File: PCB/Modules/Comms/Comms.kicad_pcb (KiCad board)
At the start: 4 copper layers, 50 x 50 mm, 26 parts, among them J1 In, J2 ESP32, J3 Bus, J4 Bus, SW1 RUN/~{PROG}, U1 DS1390U, U2 THVD1420D, U3 WiFi / BLE, Y1 32.767kHz

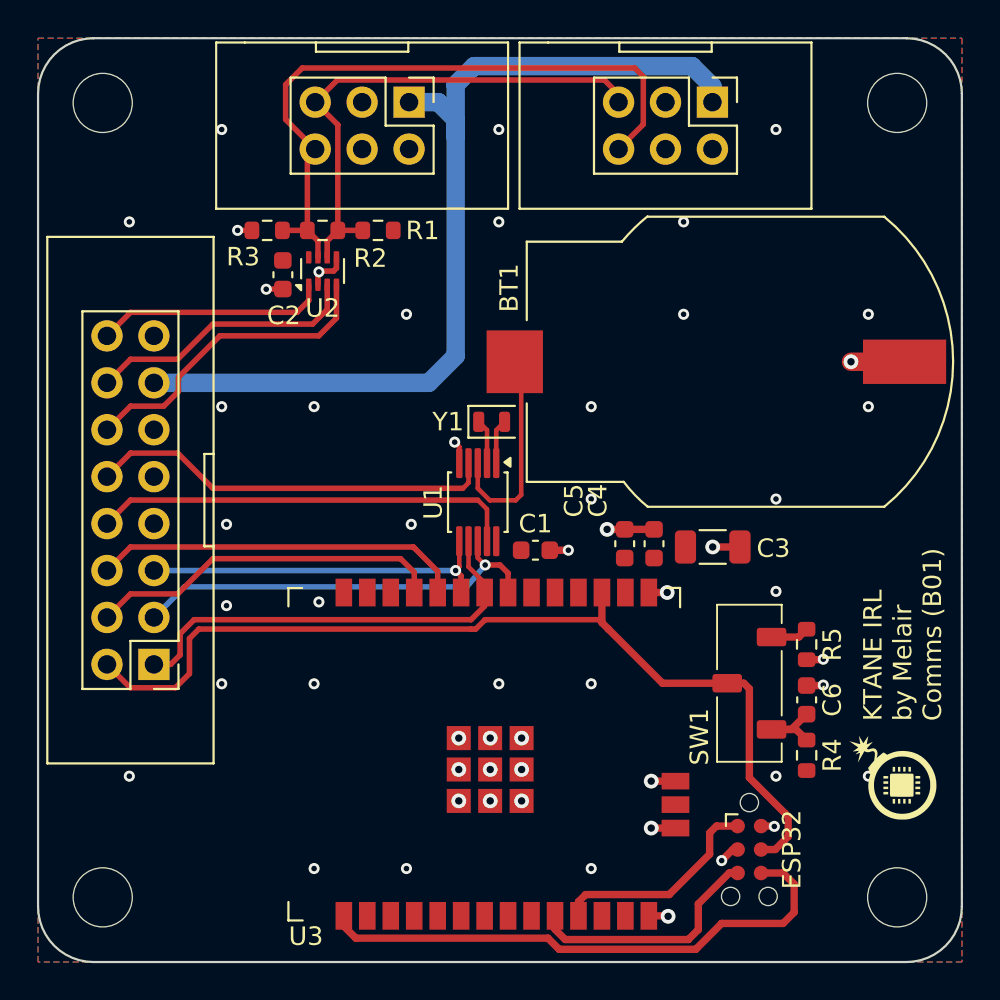
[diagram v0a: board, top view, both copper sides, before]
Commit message: Add ESD protection to the RS485 networks.
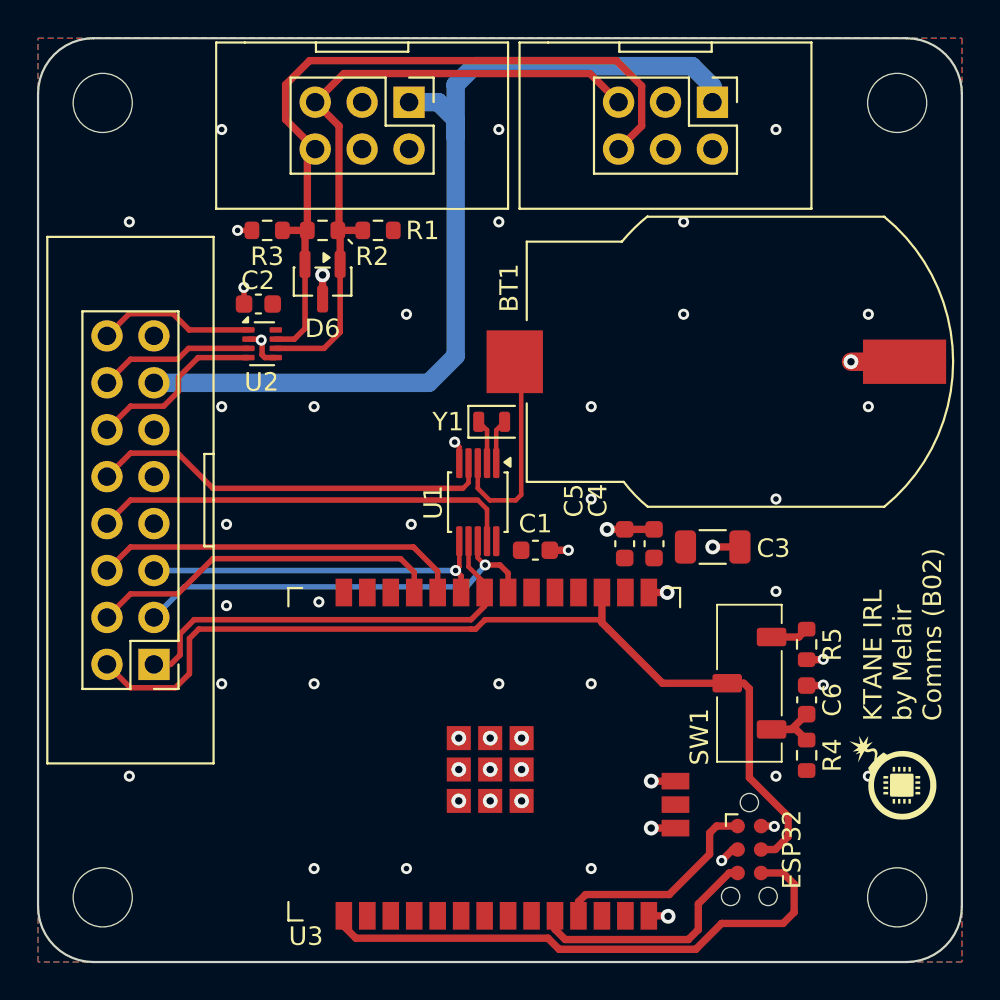
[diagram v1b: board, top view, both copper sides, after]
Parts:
- added D6: T24CAN, Package_TO_SOT_SMD:SOT-23, F.Cu at (35.4, 33.2)
- R1, R3: value 470 -> 430
- moved U2 5.12 mm to (32.1, 36.5), turned to 0 degrees
- moved C2 2.07 mm to (31.9, 34.4), turned to 180 degrees
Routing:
- net A: track 28.2 -> 36.0 mm
- net BUS-TX: track 17.2 -> 9.72 mm
- net BUS-DE: track 14.9 -> 8.43 mm
- net B: track 36.2 -> 41.6 mm
- net BUS-RX: track 12.6 -> 8.52 mm
- net GND: track 20.8 -> 22.1 mm, vias 37 -> 38
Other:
- board text added: "KTANE IRL by Melair Comms (B02)"
- board text removed: "KTANE IRL by Melair Comms (B01)"

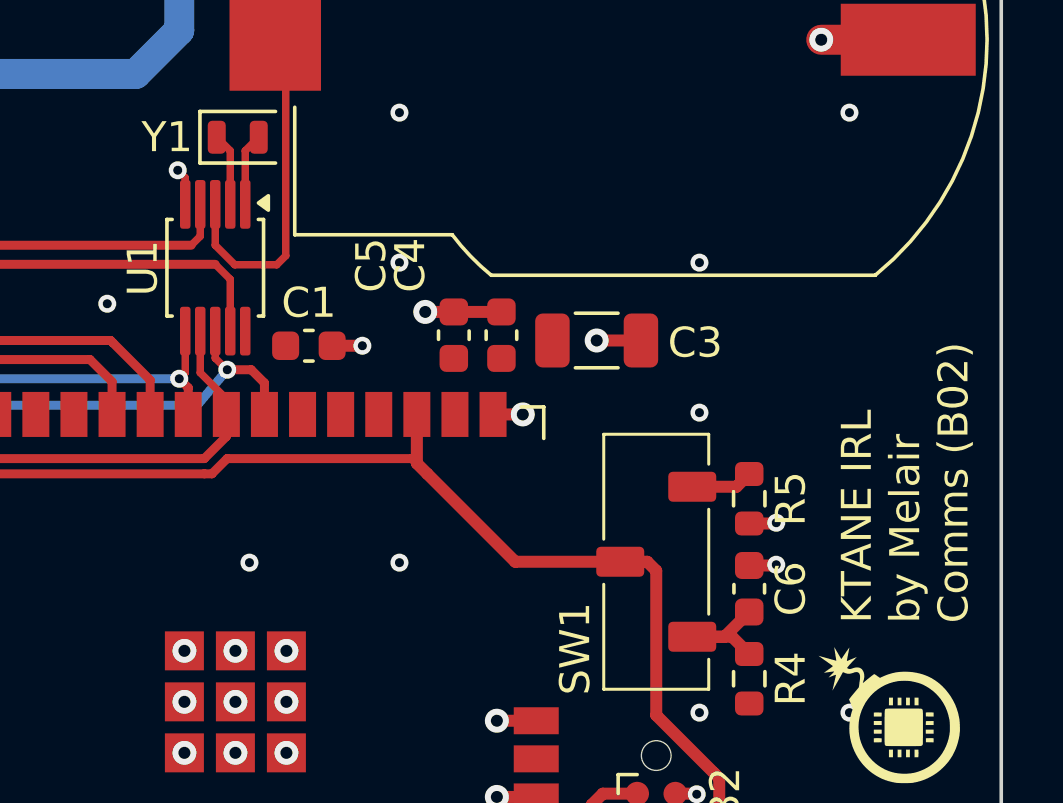
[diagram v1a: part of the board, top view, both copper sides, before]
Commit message: Include all corrections, mint new gerbers. Update some to KiCad 10.
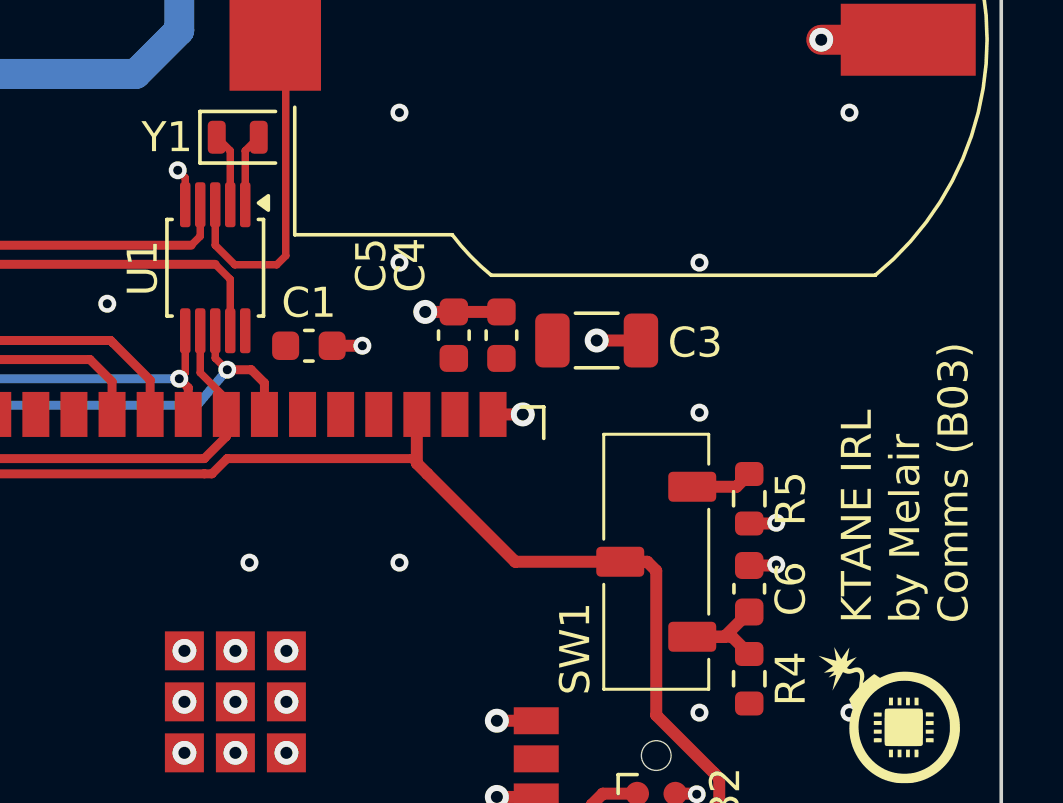
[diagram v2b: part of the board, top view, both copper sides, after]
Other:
- board text added: "KTANE IRL by Melair Comms (B03)"
- board text removed: "KTANE IRL by Melair Comms (B02)"

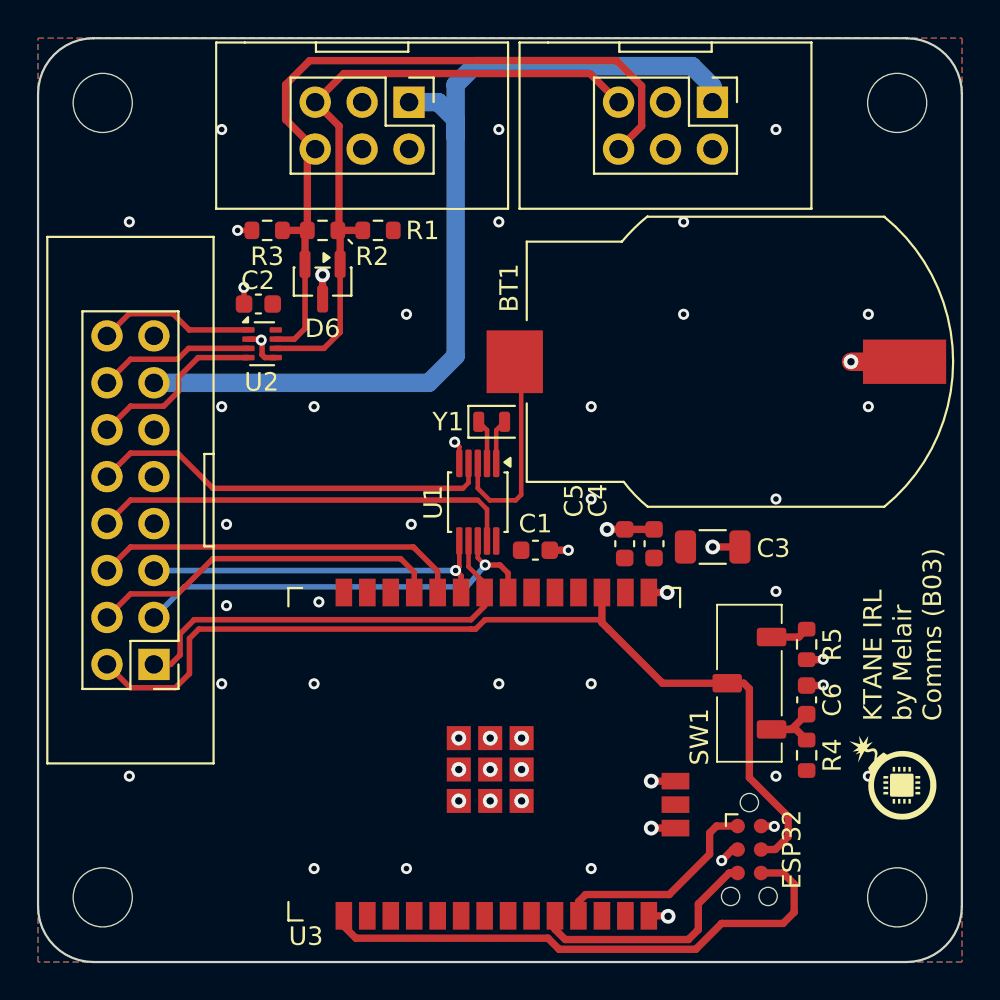
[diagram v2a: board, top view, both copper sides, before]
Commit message: feat: Rework comms board to have an STM32 for communications.
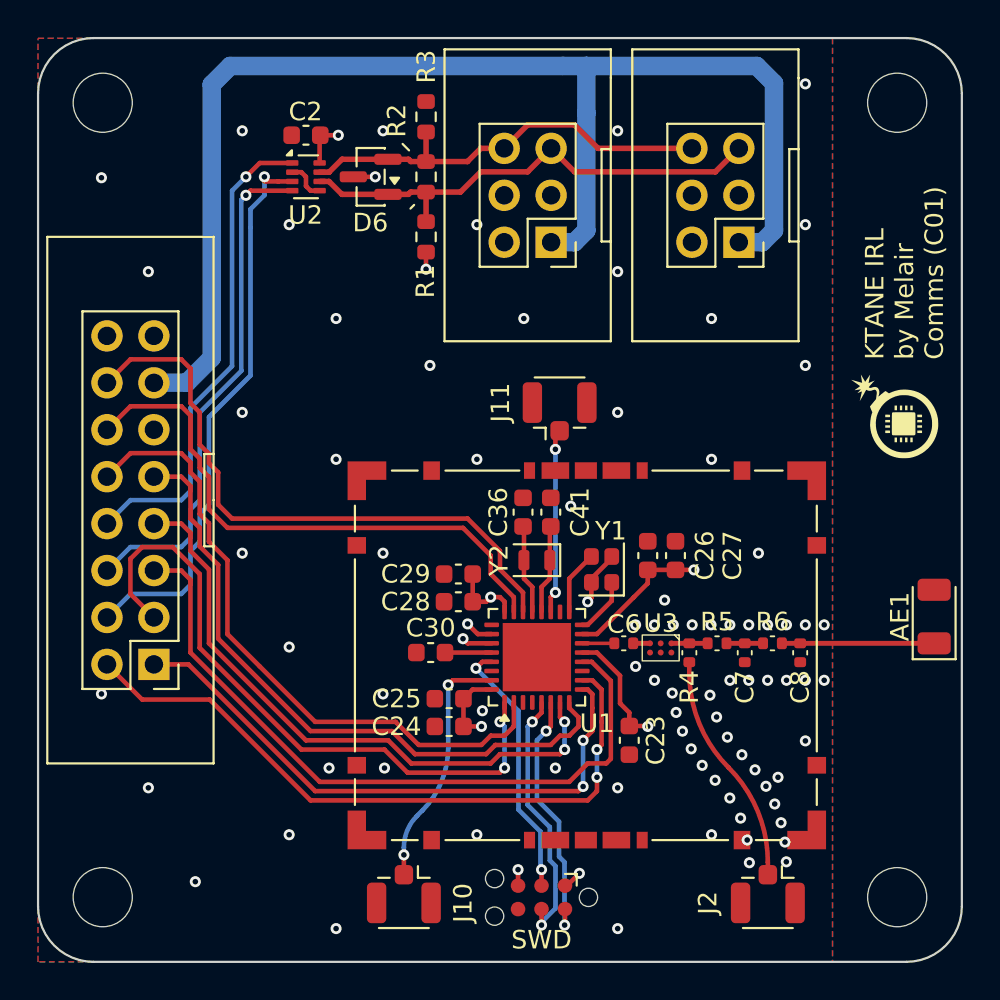
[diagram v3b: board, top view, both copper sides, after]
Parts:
- removed BT1: CR2032, KTANE:CellHolder
- removed C1: 0.1μF, Capacitor_SMD:C_0603_1608Metric
- removed C3: 22uF, Capacitor_SMD:C_1206_3216Metric
- removed C4: 47uF, Capacitor_SMD:C_0603_1608Metric
- removed C5: 0.1uF, Capacitor_SMD:C_0603_1608Metric
- removed SW1: RUN/~{PROG}, KTANE:JS102011JCQN
- added AE1: 2450AT18A0100001E, RF_Antenna:Johanson_2450AT18x100_2400-2500Mhz, F.Cu at (68.5, 51.3)
- added C23: 0.1μF, Capacitor_SMD:C_0603_1608Metric, F.Cu at (52.0, 58.0)
- added C24: 0.1μF, Capacitor_SMD:C_0603_1608Metric, F.Cu at (42.2, 57.2)
- added C25: 4.7uF, Capacitor_SMD:C_0603_1608Metric, F.Cu at (42.2, 55.8)
- added C26: 0.1μF, Capacitor_SMD:C_0603_1608Metric, F.Cu at (53.0, 48.0)
- added C27: 100pF, Capacitor_SMD:C_0603_1608Metric, F.Cu at (54.5, 48.0)
- added C28: 0.1μF, Capacitor_SMD:C_0603_1608Metric, F.Cu at (42.8, 50.5)
- added C29: 4.7uF, Capacitor_SMD:C_0603_1608Metric, F.Cu at (42.8, 49.0)
- added C30: 0.1μF, Capacitor_SMD:C_0603_1608Metric, F.Cu at (41.2, 53.2)
- added C36: 8pF, Capacitor_SMD:C_0603_1608Metric, F.Cu at (46.2, 45.6)
- added C41: 8pF, Capacitor_SMD:C_0603_1608Metric, F.Cu at (47.8, 45.6)
- added C7: ~, KTANE:R_0402_1005Metric_Tweaked, F.Cu at (58.2, 53.3)
- added C8: ~, KTANE:R_0402_1005Metric_Tweaked, F.Cu at (61.2, 53.3)
- added J10: 1PPS In, Connector_Coaxial:U.FL_Hirose_U.FL-R-SMT-1_Vertical, F.Cu at (39.8, 66.8)
- added J11: 32MHz Out, Connector_Coaxial:U.FL_Hirose_U.FL-R-SMT-1_Vertical, F.Cu at (48.2, 39.7)
- added J12: Shield, KTANE:EMI_Shield_Straight, F.Cu at (49.6, 63.4)
- added J13: Shield, KTANE:EMI_Shield_Straight, F.Cu at (49.6, 43.4)
- added J5: SWD, Connector:Tag-Connect_TC2030-IDC-NL_2x03_P1.27mm_Vertical, F.Cu at (47.2, 66.5)
- added J6: Shield, KTANE:EMI_Shield_Corner, F.Cu at (62.1, 43.4)
- added J7: Shield, KTANE:EMI_Shield_Corner, F.Cu at (37.2, 43.4)
- added J8: Shield, KTANE:EMI_Shield_Corner, F.Cu at (37.2, 63.4)
- added J9: Shield, KTANE:EMI_Shield_Corner, F.Cu at (62.1, 63.4)
- added R6: 0, KTANE:R_0402_1005Metric_Tweaked, F.Cu at (59.8, 52.8)
- added Y2: 32.768k, Crystal:Crystal_SMD_2012-2Pin_2.0x1.2mm, F.Cu at (47.0, 48.2)
- C6: value 0.1μF -> 20pF; footprint Capacitor_SMD:C_0603_1608Metric -> KTANE:R_0402_1005Metric_Tweaked
- H1, H2, H3, H4: footprint MountingHole:MountingHole_3.2mm_M3 -> KTANE:MountingHole_3.2mm_M3_NoCopper
- J2: value ESP32 -> Test; footprint Connector:Tag-Connect_TC2030-IDC-NL_2x03_P1.27mm_Vertical -> Connector_Coaxial:U.FL_Hirose_U.FL-R-SMT-1_Vertical
- R4, R5: value 10k -> 0; footprint Resistor_SMD:R_0603_1608Metric -> KTANE:R_0402_1005Metric_Tweaked
- U1: value DS1390U -> STM32WB09KEVx; footprint Package_SO:MSOP-10_3x3mm_P0.5mm -> Package_DFN_QFN:QFN-32-1EP_5x5mm_P0.5mm_EP3.7x3.7mm
- U3: value WiFi / BLE -> MLPF-NRG-01D3; footprint KTANE:ESP32-C5-WROOM-1U -> KTANE:MLPF-NRG-01D3
- Y1: value 32.767kHz -> 32MHz; footprint Crystal:Crystal_SMD_2012-2Pin_2.0x1.2mm -> Crystal:Crystal_SMD_2016-4Pin_2.0x1.6mm
- moved G*** 19.6 mm to (66.4, 40.4)
- moved U3 11.0 mm to (53.7, 53.0)
- moved R3 10.6 mm to (41.0, 24.2), turned to 90 degrees
- moved C6 10.4 mm to (51.7, 52.8), turned to 180 degrees
- moved Y1 9.96 mm to (50.5, 48.8), turned to 90 degrees
- moved J3 9.72 mm to (46.5, 28.5), turned to 180 degrees
- moved C2 9.49 mm to (34.5, 25.2)
- moved U2 9.34 mm to (34.5, 27.5)
- moved U1 8.98 mm to (47.0, 53.5), turned to 90 degrees
- moved R4 8.43 mm to (55.2, 53.3)
- moved R2 6.31 mm to (41.0, 27.5), turned to 90 degrees
- moved D6 6.24 mm to (38.0, 27.5), turned to 180 degrees
- moved R5 4.85 mm to (56.8, 52.8), turned to 0 degrees
- moved J4 4.64 mm to (56.7, 28.5), turned to 180 degrees
- moved J2 3.06 mm to (59.5, 66.8)
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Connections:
- C6 pad 1: Net-(SW1-A) -> Net-(U3-IN)
- C6 pad 2: GND -> Net-(U1-RF1)
- J1 pad 10: ~{RTC-CS} -> ~{BLE_INT}
- J1 pad 12: BUS-TX -> BLE-UART-TX
- J1 pad 14: BUS-DE -> BLE-UART-RX
- J1 pad 16: BUS-RX -> unconnected-(J1-I7-Pad16)
- J1 pad 2: ESP32-EN -> ~{SPI-CS}
- J1 pad 4: ~{ESP32-INT} -> BUS-DE
- J1 pad 6: ~{ESP32-CS} -> BUS-TX
- J1 pad 7: unconnected-(J1-SDA-Pad7) -> SDA
- J1 pad 8: ~{RTC-INT} -> BUS-RX
- J1 pad 9: unconnected-(J1-SCL-Pad9) -> SCL
- J2 pad 1: ESP32-PROG-TX -> Net-(J2-Pin_1)
- J2 pad 2: +3.3V -> (no net)
- R4 pad 1: +3.3V -> Net-(J2-Pin_1)
- R4 pad 2: Net-(SW1-A) -> Net-(U3-OUT)
- R5 pad 1: Net-(SW1-C) -> Net-(U3-OUT)
- R5 pad 2: GND -> Net-(C7-Pad1)
- U1 pad 1: Net-(U1-X1) -> SPI-CLK
- U1 pad 10: +3.3V -> ~{SPI-CS}
- U1 pad 2: Net-(U1-X2) -> ~{BLE_INT}
- U1 pad 3: +BATT -> unconnected-(U1-PB1-Pad3)
- U1 pad 4: ~{RTC-CS} -> unconnected-(U1-PB0-Pad4)
- U1 pad 5: GND -> SWCLK
- U1 pad 6: SPI-COPI -> SWDIO
- U1 pad 7: SPI-CIPO -> SDA
- U1 pad 8: SPI-CLK -> SCL
- U1 pad 9: ~{RTC-INT} -> SPI-CIPO
- Y1 pad 1: Net-(U1-X2) -> Net-(U1-OSCOUT)
- Y1 pad 2: Net-(U1-X1) -> GND
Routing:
- net ESP32-EN: track 52.7 -> 0.00 mm
- net ~{SPI-CS}: track 0.00 -> 36.6 mm, vias 0 -> 2
- net SCL: track 0.00 -> 35.3 mm
- net ~{BLE_INT}: track 0.00 -> 35.1 mm
- net SDA: track 0.00 -> 33.8 mm, vias 0 -> 2
- net BLE-UART-RX: track 0.00 -> 33.3 mm
- net BLE-UART-TX: track 0.00 -> 30.6 mm
- net BOOT0: track 29.8 -> 0.00 mm
- net +3.3V: track 0.72 -> 28.7 mm, vias 18 -> 8
- net ~{RTC-INT}: track 23.0 -> 0.00 mm
- net BUS-DE: track 8.43 -> 31.0 mm, vias 0 -> 1
- net ~{RTC-CS}: track 22.1 -> 0.00 mm
- net ~{ESP32-CS}: track 20.1 -> 0.00 mm
- net +5V: track 51.1 -> 70.9 mm
- net ~{ESP32-INT}: track 19.3 -> 0.00 mm
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- added copper zone on In2.Cu, net +3.3V
- added copper zone on B.Cu, net GND
- added copper zone on F.Cu, net GND
- removed copper zone on B.Cu, net +3.3V
- removed copper zone on F.Cu, net +3.3V
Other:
- board text added: "KTANE IRL by Melair Comms (C01)"
- board text removed: "KTANE IRL by Melair Comms (B03)"

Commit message: feat: Add support for battery for RTC on comms board.
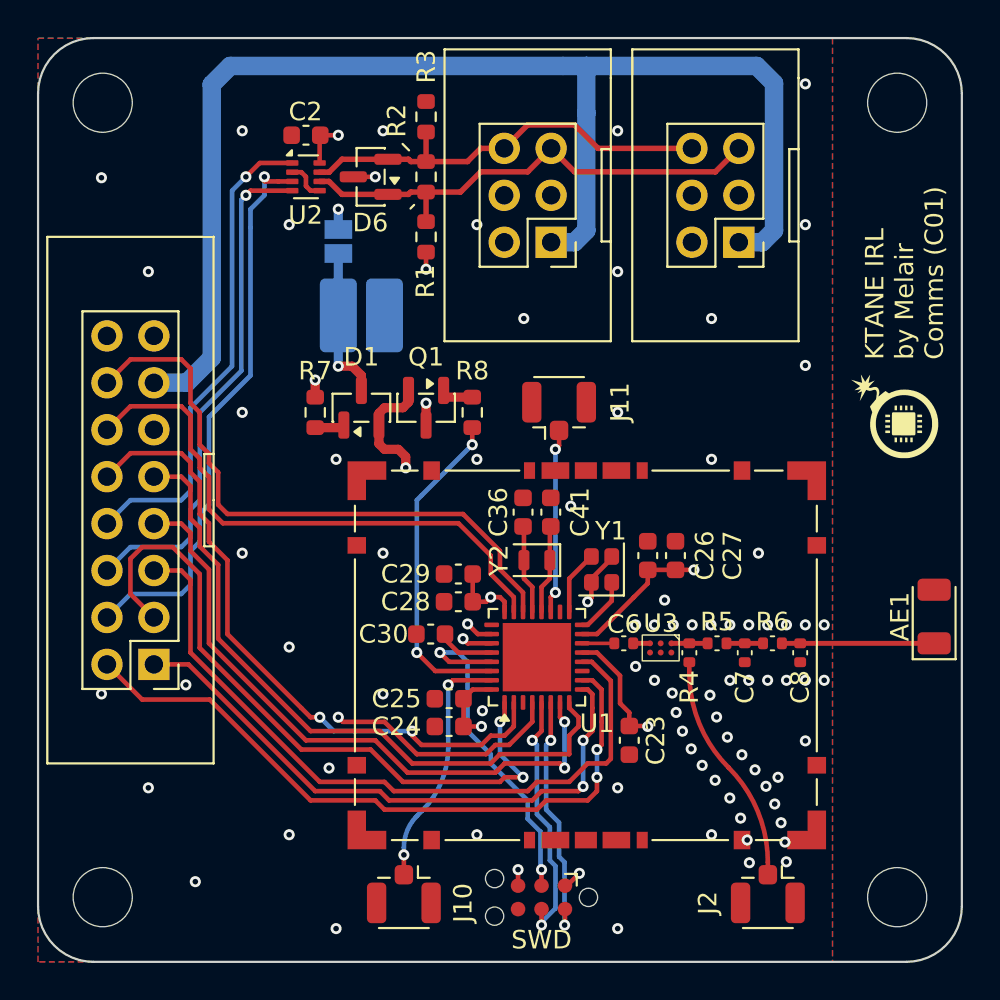
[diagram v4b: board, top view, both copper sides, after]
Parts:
- added D1: BAT54S, Package_TO_SOT_SMD:SOT-23, F.Cu at (37.5, 40.0)
- added J14: BATT +, KTANE:Pad4x2, B.Cu at (36.2, 35.0)
- added J15: BATT -, KTANE:Pad4x2, B.Cu at (38.8, 35.0)
- added JP1: NO BATT, Jumper:SolderJumper-2_P1.3mm_Open_Pad1.0x1.5mm, B.Cu at (36.2, 31.0)
- added Q1: Q_PMOS_GSD, Package_TO_SOT_SMD:SOT-23, F.Cu at (41.0, 40.0)
- added R7: 1000, Resistor_SMD:R_0603_1608Metric, F.Cu at (35.0, 40.2)
- added R8: 120, Resistor_SMD:R_0603_1608Metric, F.Cu at (43.5, 40.2)
- moved C30 1.00 mm to (41.2, 52.2)
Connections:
- C23 pad 1: +3.3V -> +3.3VP
- C24 pad 1: +3.3V -> +3.3VP
- C25 pad 1: +3.3V -> +3.3VP
- C26 pad 1: +3.3V -> +3.3VP
- C27 pad 1: +3.3V -> +3.3VP
- C28 pad 1: +3.3V -> +3.3VP
- C29 pad 1: +3.3V -> +3.3VP
- J10 pad 2: (no net) -> GND
- J11 pad 2: (no net) -> GND
- J2 pad 2: (no net) -> GND
- J5 pad 1: +3.3V -> +3.3VP
- U1 pad 13: +3.3V -> +3.3VP
- U1 pad 15: +3.3V -> +3.3VP
- U1 pad 24: +3.3V -> +3.3VP
- U1 pad 27: +3.3V -> +3.3VP
- U1 pad 30: unconnected-(U1-PB5-Pad30) -> ~{RUN}
- U1 pad 32: +3.3V -> +3.3VP
- U1 pad 4: unconnected-(U1-PB0-Pad4) -> +3.3V
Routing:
- net +3.3VP: track 0.00 -> 31.8 mm, vias 0 -> 7
- net ~{RUN}: track 0.00 -> 17.9 mm, vias 0 -> 2
- net +3.3V: track 28.7 -> 19.7 mm, vias 8 -> 6
- net Net-(D1-COM): track 0.00 -> 8.37 mm, vias 0 -> 1
- net ~{RESET}: track 14.4 -> 18.5 mm
- net SPI-CLK: track 35.6 -> 37.7 mm
- net Net-(D1-A): track 0.00 -> 1.61 mm
- net Net-(Q1-G): track 0.00 -> 1.53 mm
- net SDA: track 33.8 -> 35.0 mm
- net SCL: track 35.3 -> 36.3 mm
- net Net-(U1-VDDA_VCAP): track 2.52 -> 3.10 mm
- net ~{BLE_INT}: track 35.1 -> 35.2 mm, vias 0 -> 2
- net GND: vias 85 -> 82
- added copper zone on In2.Cu, net +3.3VP
